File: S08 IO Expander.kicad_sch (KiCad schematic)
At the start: 11 parts, among them U11 PCAL9714

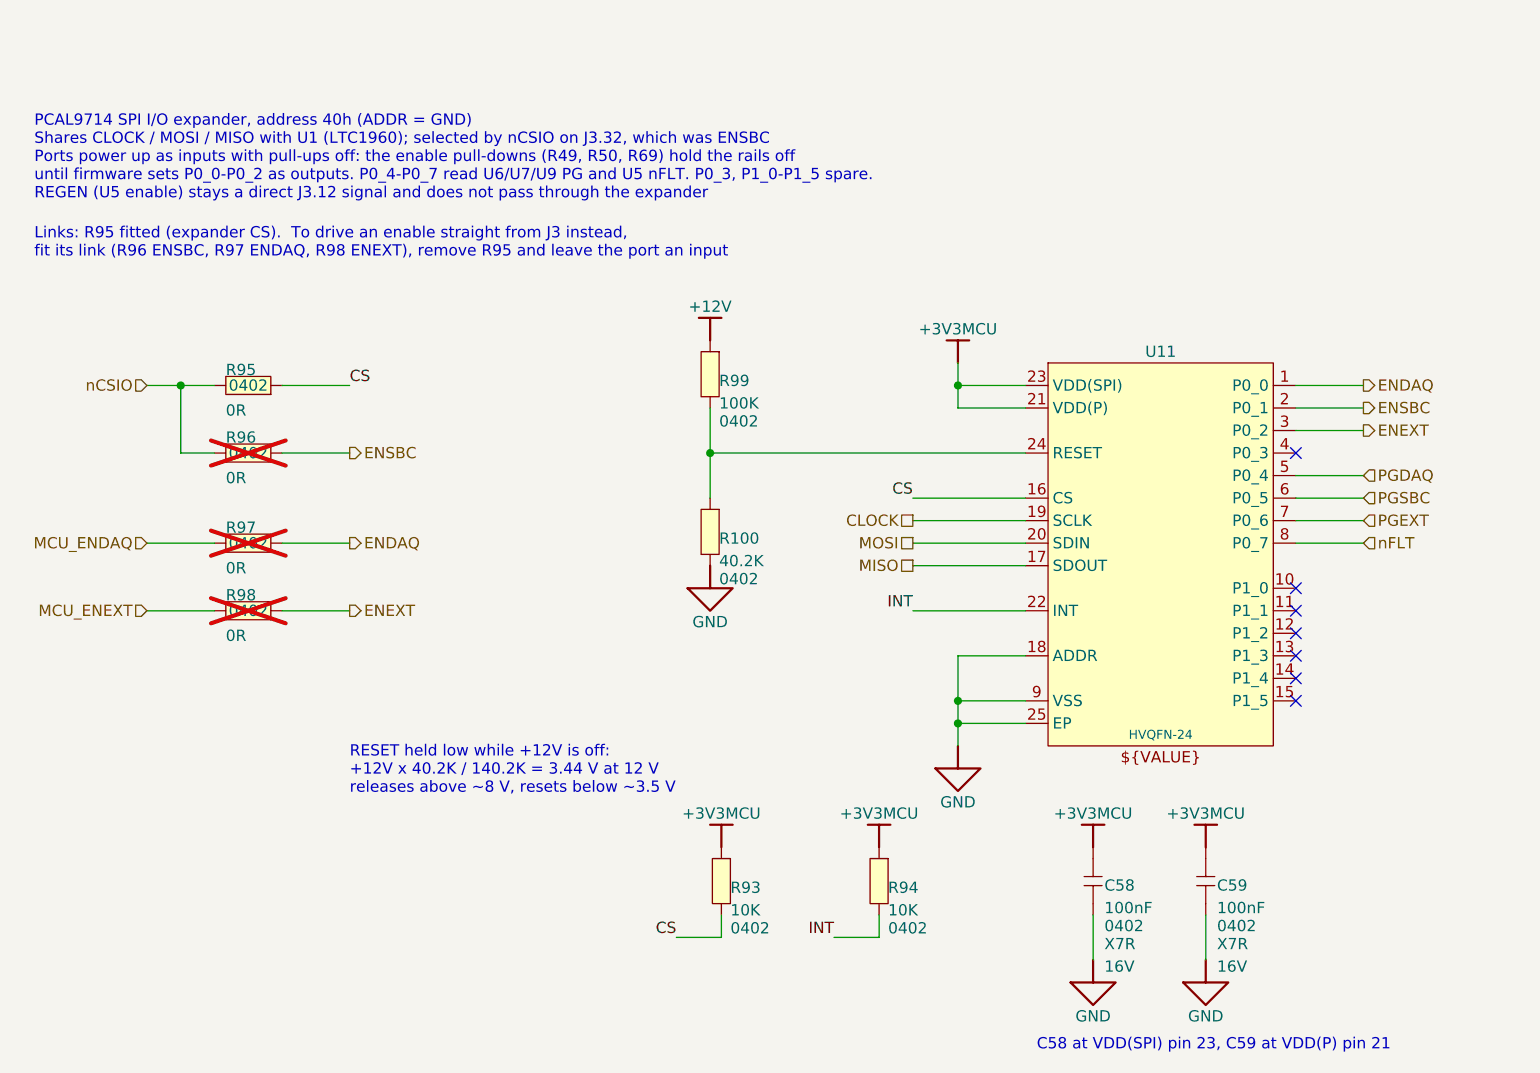
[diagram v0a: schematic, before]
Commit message: Drive the expander RESET through a FET and use BSS138 for Q20-Q23
The +12V divider on U11 RESET could back-power the expander and gave a
weak logic high. Q23 now passes +3V3MCU to RESET while +12V is up, with
its gate fed by R99 100K / R101 1M. R100 (now 100K) holds RESET low when
+12V is off, and RESET can no longer rise above +3V3MCU.

Q20-Q23 are now onsemi BSS138 in SOT-23, replacing the DFN1006
DMN65D8LFB-7. The BSS138 has no gate zener, so gate leakage is at most
100 nA on the 100K PG pull-ups and the Q23 gate divider. The README
warns against ESD-protected substitutes.

The root sheet change is KiCad reordering items only.

Co-Authored-By: Claude Opus 5.5 <noreply@anthropic.com>
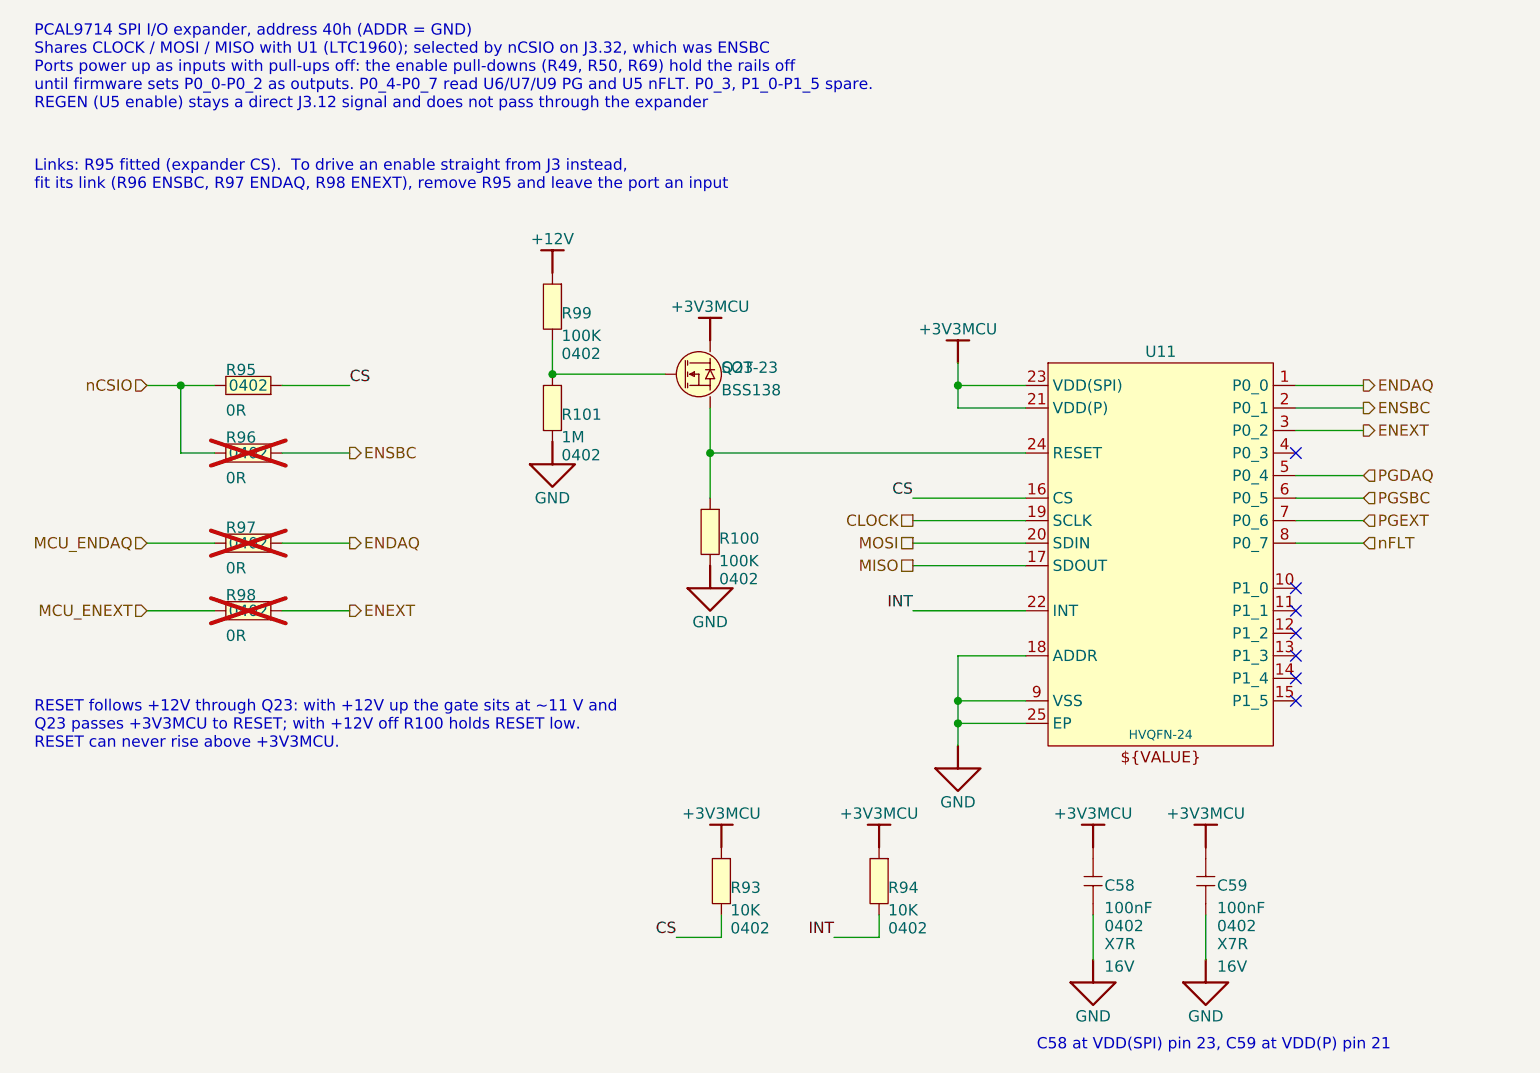
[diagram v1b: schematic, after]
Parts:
- removed R100: 40.2K, Resistor_SMD:R_0402_1005Metric, symbol Lattech Systems:Resistor 40.2K 1% 0402
- added Q23: BSS138, Package_TO_SOT_SMD:SOT-23, symbol Lattech Systems:Transistor N-Channel MOSFET 50V BSS138 SOT-23
- added R100: 100K, Resistor_SMD:R_0402_1005Metric, symbol Lattech Systems:Resistor 100K 1% 0402
- added R101: 1M, Resistor_SMD:R_0402_1005Metric, symbol Lattech Systems:Resistor 1M 1% 0402
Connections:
- net +3V3MCU: now also Q23.3 (D)
- net GND: now also R100.1, R101.1
- net at R99.1: now also Q23.1 (G), R101.2; no longer U11.24 (RESET)
- new net: Q23.2 (S), R100.2, U11.24 (RESET)
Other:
- note added: "RESET follows +12V through Q23: with +12V up the gate sits at ~11 V and Q23 passes +3V3MCU to RESET; with +12V off R100 holds RESET low. RESET can never rise above +3V3MCU."
- note removed: "RESET held low while +12V is off: +12V x 40.2K / 140.2K = 3.44 V at 12 V releases above ~8 V, resets below ~3.5 V"

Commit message: BOM consolidation, OVLO divider to 1%, U5 fixes and I2C config option
- Consolidate passives: 1uF 50V to 0603, 100nF to 50V X7R 0402,
  10uF to 50V X7R 1210, 220nF to 0603, 10R to 0402 (100 -> 90 BOM lines)
- TPS22811 OVLO divider 1M/102K 0.1% -> 1M/100K 1% (12.6V min trip)
- U5 LM51772: C30 -> R102 10K to GND (VCC1 disabled), C32 -> 22uF 16V 0805,
  R29 1.9K -> 1.87K to sit inside the CFG4 window
- Add DNP I2C configuration option for U5 (R103-R107) on J3.34/J3.36,
  shared with R97/R98 fallback
- Document all changes in README.md

Co-Authored-By: Claude Opus 5.5 <noreply@anthropic.com>
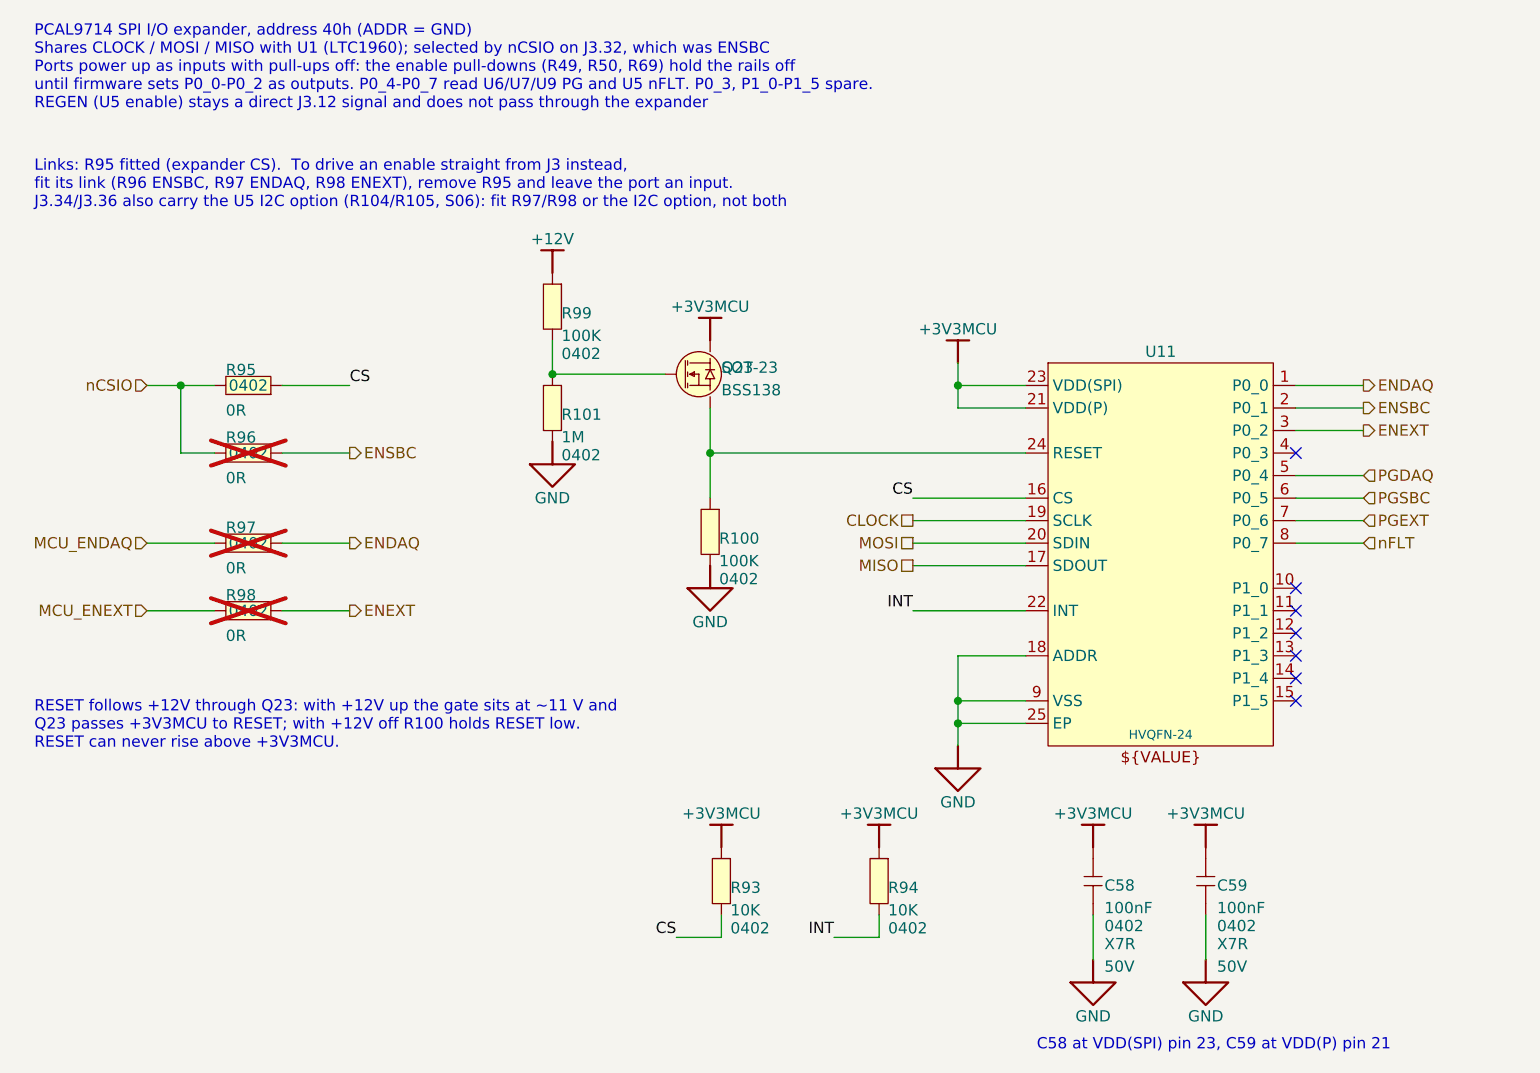
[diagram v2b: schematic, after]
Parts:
- C58, C59: symbol Lattech Systems:Capacitor 100nF 16V X7R 0402 -> Lattech Systems:Capacitor 100nF 50V X7R 0402; MANUFACTURER ? -> Yageo; MANUFACTURER_PN ? -> CC0402KPX7R9BB104; VOLTAGE 16V -> 50V
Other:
- note added: "Links: R95 fitted (expander CS). To drive an enable straight from J3 instead, fit its link (R96 ENSBC, R97 ENDAQ, R98 ENEXT), remove R95 and leave the port an input. J3.34/J3.36 also carry the U5 I2C option (R104/R105, S06): fit R97/R98 or the I2C option, not both"
- note removed: "Links: R95 fitted (expander CS). To drive an enable straight from J3 instead, fit its link (R96 ENSBC, R97 ENDAQ, R98 ENEXT), remove R95 and leave the port an input"
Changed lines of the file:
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@@
 	(generator_version "10.0")
 	(paper "A3")
-	(text "Links: R95 fitted (expander CS).  To drive an enable straight from J3 instead,\nfit its link (R96 ENSBC, R97 ENDAQ, R98 ENEXT), remove R95 and leave the port an input"
+	(text "Links: R95 fitted (expander CS).  To drive an enable straight from J3 instead,\nfit its link (R96 ENSBC, R97 ENDAQ, R98 ENEXT), remove R95 and leave the port an input.\nJ3.34/J3.36 also carry the U5 I2C option (R104/R105, S06): fit R97/R98 or the I2C option, not both"
 		(exclude_from_sim no)
 		(at 63.5 81.28 0)
@@
 	)
 	(symbol
-		(lib_id "Lattech Systems:Capacitor 100nF 16V X7R 0402")
+		(lib_id "Lattech Systems:Capacitor 100nF 50V X7R 0402")
 		(at 195.58 162.56 90)
 		(unit 1)
@@
 			)
 		)
-		(property "Description" "Capacitor 100nF 16V X7R 0402"
+		(property "Description" "Capacitor 100nF 50V X7R 0402"
 			(at 195.58 162.56 0)
 			(hide yes)
@@
 			)
 		)
-		(property "MANUFACTURER" "?"
+		(property "MANUFACTURER" "Yageo"
 			(at 194.31 158.242 90)
 			(hide yes)
@@
 			)
 		)
-		(property "MANUFACTURER_PN" "?"
+		(property "MANUFACTURER_PN" "CC0402KPX7R9BB104"
 			(at 194.31 158.242 90)
 			(hide yes)
@@
 			)
 		)
-		(property "VOLTAGE" "16V"
+		(property "VOLTAGE" "50V"
 			(at 196.85 171.45 90)
 			(show_name no)
@@
 	)
 	(symbol
-		(lib_id "Lattech Systems:Capacitor 100nF 16V X7R 0402")
+		(lib_id "Lattech Systems:Capacitor 100nF 50V X7R 0402")
 		(at 182.88 162.56 90)
 		(unit 1)
@@
 			)
 		)
-		(property "Description" "Capacitor 100nF 16V X7R 0402"
+		(property "Description" "Capacitor 100nF 50V X7R 0402"
 			(at 182.88 162.56 0)
 			(hide yes)
@@
 			)
 		)
-		(property "MANUFACTURER" "?"
+		(property "MANUFACTURER" "Yageo"
 			(at 181.61 158.242 90)
 			(hide yes)
@@
 			)
 		)
-		(property "MANUFACTURER_PN" "?"
+		(property "MANUFACTURER_PN" "CC0402KPX7R9BB104"
 			(at 181.61 158.242 90)
 			(hide yes)
@@
 			)
 		)
-		(property "VOLTAGE" "16V"
+		(property "VOLTAGE" "50V"
 			(at 184.15 171.45 90)
 			(show_name no)
